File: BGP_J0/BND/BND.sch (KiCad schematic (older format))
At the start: 5 parts, among them J1 Conn_01x13, J2 Conn_01x03, J4 Conn_01x02, J5 Conn_01x03, P7 CONN_01X04

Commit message: Updates
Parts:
- P7: footprint (none) -> Connectors_JST:JST_PH_B4B-PH-K_04x2.00mm_Straight
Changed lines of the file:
@@
 	5450 3950 5200 3950
 $Comp
-L Earth #PWR03
+L Earth #PWR01
 U 1 1 5AE4ECAD
 P 5200 4650
-F 0 "#PWR03" H 5200 4400 50  0001 C CNN
+F 0 "#PWR01" H 5200 4400 50  0001 C CNN
 F 1 "Earth" H 5200 4500 50  0001 C CNN
 F 2 "" H 5200 4650 50  0001 C CNN
@@
 BT_O
 $Comp
-L Earth #PWR04
+L Earth #PWR02
 U 1 1 5AE4F0BF
 P 6600 4250
-F 0 "#PWR04" H 6600 4000 50  0001 C CNN
+F 0 "#PWR02" H 6600 4000 50  0001 C CNN
 F 1 "Earth" H 6600 4100 50  0001 C CNN
 F 2 "" H 6600 4250 50  0001 C CNN
@@
 $EndComp
 $Comp
-L Earth #PWR05
+L Earth #PWR03
 U 1 1 5AE533F6
 P 6050 3450
-F 0 "#PWR05" H 6050 3200 50  0001 C CNN
+F 0 "#PWR03" H 6050 3200 50  0001 C CNN
 F 1 "Earth" H 6050 3300 50  0001 C CNN
 F 2 "" H 6050 3450 50  0001 C CNN
@@
 $EndComp
 $Comp
-L Earth #PWR06
+L Earth #PWR04
 U 1 1 5AE53416
 P 6600 3650
-F 0 "#PWR06" H 6600 3400 50  0001 C CNN
+F 0 "#PWR04" H 6600 3400 50  0001 C CNN
 F 1 "Earth" H 6600 3500 50  0001 C CNN
 F 2 "" H 6600 3650 50  0001 C CNN
@@
 F 0 "P7" H 6400 4350 50  0000 C CNN
 F 1 "CONN_01X04" H 6400 3850 50  0000 C CNN
-F 2 "" H 6400 4100 50  0000 C CNN
+F 2 "Connectors_JST:JST_PH_B4B-PH-K_04x2.00mm_Straight" H 6400 4100 50  0001 C CNN
 F 3 "" H 6400 4100 50  0000 C CNN
 	1    6400 4100

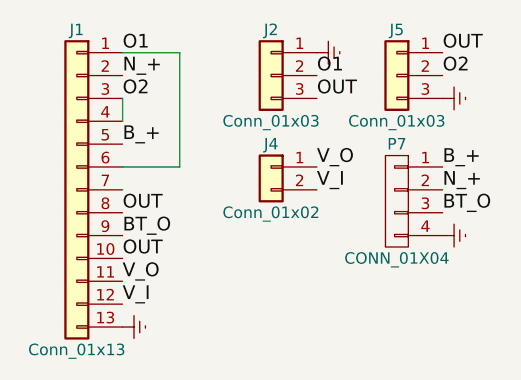
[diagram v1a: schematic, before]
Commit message: Ready to go
Reverted J0_BND  to include P/U inputs
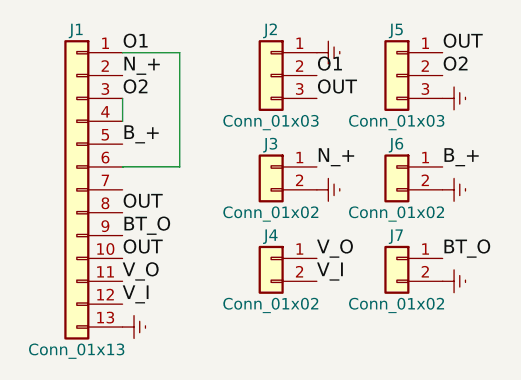
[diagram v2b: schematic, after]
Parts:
- removed P7: CONN_01X04, Connectors_JST:JST_PH_B4B-PH-K_04x2.00mm_Straight, symbol CONN_01X04
- added J3, J6: Conn_01x02, LIBS:TerminalBlock_Phoenix_MPT-2.54mm_2pol, symbol Conn_01x02
- added J7: Conn_01x02, Connectors_JST:JST_PH_B2B-PH-K_02x2.00mm_Straight, symbol Conn_01x02
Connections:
- net BT_O: now also J7.1 (Pin_1)
- net B_+: now also J6.1 (Pin_1)
- net Earth: now also J3.2 (Pin_2), J6.2 (Pin_2), J7.2 (Pin_2)
- net N_+: now also J3.1 (Pin_1)
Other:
- moved on the sheet: J4
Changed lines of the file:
@@
 LIBS:switches
 LIBS:relays
+LIBS:motors
 LIBS:transistors
 LIBS:conn
@@
 	-1   0    0    -1
 $EndComp
-Text Label 6600 4050 0    60   ~ 0
+$Comp
+L Conn_01x02 J3
+U 1 1 5AE4EB53
+P 5850 3950
+F 0 "J3" H 5850 4050 50  0000 C CNN
+F 1 "Conn_01x02" H 5850 3750 50  0000 C CNN
+F 2 "LIBS:TerminalBlock_Phoenix_MPT-2.54mm_2pol" H 5850 3950 50  0001 C CNN
+F 3 "" H 5850 3950 50  0001 C CNN
+	1    5850 3950
+	-1   0    0    -1
+$EndComp
+$Comp
+L Conn_01x02 J6
+U 1 1 5AE4EB86
+P 6400 3950
+F 0 "J6" H 6400 4050 50  0000 C CNN
+F 1 "Conn_01x02" H 6400 3750 50  0000 C CNN
+F 2 "LIBS:TerminalBlock_Phoenix_MPT-2.54mm_2pol" H 6400 3950 50  0001 C CNN
+F 3 "" H 6400 3950 50  0001 C CNN
+	1    6400 3950
+	-1   0    0    -1
+$EndComp
+Text Label 6050 3950 0    60   ~ 0
 N_+
 Text Label 5200 3550 0    60   ~ 0
 N_+
+$Comp
+L Earth #PWR01
+U 1 1 5AE4EC05
+P 6050 4050
+F 0 "#PWR01" H 6050 3800 50  0001 C CNN
+F 1 "Earth" H 6050 3900 50  0001 C CNN
+F 2 "" H 6050 4050 50  0001 C CNN
+F 3 "" H 6050 4050 50  0001 C CNN
+	1    6050 4050
+	0    -1   1    0
+$EndComp
+$Comp
+L Earth #PWR02
+U 1 1 5AE4EC20
+P 6600 4050
+F 0 "#PWR02" H 6600 3800 50  0001 C CNN
+F 1 "Earth" H 6600 3900 50  0001 C CNN
+F 2 "" H 6600 4050 50  0001 C CNN
+F 3 "" H 6600 4050 50  0001 C CNN
+	1    6600 4050
+	0    -1   1    0
+$EndComp
 Wire Wire Line
 	5200 3650 5200 3750
@@
 	5450 3950 5200 3950
 $Comp
-L Earth #PWR01
+L Earth #PWR03
 U 1 1 5AE4ECAD
 P 5200 4650
-F 0 "#PWR01" H 5200 4400 50  0001 C CNN
+F 0 "#PWR03" H 5200 4400 50  0001 C CNN
 F 1 "Earth" H 5200 4500 50  0001 C CNN
 F 2 "" H 5200 4650 50  0001 C CNN
@@
 L Conn_01x02 J4
 U 1 1 5AE4EEB8
-P 5850 3950
-F 0 "J4" H 5850 4050 50  0000 C CNN
-F 1 "Conn_01x02" H 5850 3750 50  0000 C CNN
-F 2 "Connectors_JST:JST_PH_B2B-PH-K_02x2.00mm_Straight" H 5850 3950 50  0001 C CNN
-F 3 "" H 5850 3950 50  0001 C CNN
-	1    5850 3950
-	-1   0    0    -1
-$EndComp
-Text Label 6050 4050 0    60   ~ 0
+P 5850 4350
+F 0 "J4" H 5850 4450 50  0000 C CNN
+F 1 "Conn_01x02" H 5850 4150 50  0000 C CNN
+F 2 "Connectors_JST:JST_PH_B2B-PH-K_02x2.00mm_Straight" H 5850 4350 50  0001 C CNN
+F 3 "" H 5850 4350 50  0001 C CNN
+	1    5850 4350
+	-1   0    0    -1
+$EndComp
+Text Label 6050 4450 0    60   ~ 0
 V_I
-Text Label 6050 3950 0    60   ~ 0
+Text Label 6050 4350 0    60   ~ 0
 V_O
-Text Label 6600 4150 0    60   ~ 0
+$Comp
+L Conn_01x02 J7
+U 1 1 5AE4F048
+P 6400 4350
+F 0 "J7" H 6400 4450 50  0000 C CNN
+F 1 "Conn_01x02" H 6400 4150 50  0000 C CNN
+F 2 "Connectors_JST:JST_PH_B2B-PH-K_02x2.00mm_Straight" H 6400 4350 50  0001 C CNN
+F 3 "" H 6400 4350 50  0001 C CNN
+	1    6400 4350
+	-1   0    0    -1
+$EndComp
+Text Label 6600 4350 0    60   ~ 0
 BT_O
 $Comp
-L Earth #PWR02
+L Earth #PWR04
 U 1 1 5AE4F0BF
-P 6600 4250
-F 0 "#PWR02" H 6600 4000 50  0001 C CNN
-F 1 "Earth" H 6600 4100 50  0001 C CNN
-F 2 "" H 6600 4250 50  0001 C CNN
-F 3 "" H 6600 4250 50  0001 C CNN
-	1    6600 4250
+P 6600 4450
+F 0 "#PWR04" H 6600 4200 50  0001 C CNN
+F 1 "Earth" H 6600 4300 50  0001 C CNN
+F 2 "" H 6600 4450 50  0001 C CNN
+F 3 "" H 6600 4450 50  0001 C CNN
+	1    6600 4450
 	0    -1   -1   0
 $EndComp
@@
 $EndComp
 $Comp
-L Earth #PWR03
+L Earth #PWR05
 U 1 1 5AE533F6
 P 6050 3450
-F 0 "#PWR03" H 6050 3200 50  0001 C CNN
+F 0 "#PWR05" H 6050 3200 50  0001 C CNN
 F 1 "Earth" H 6050 3300 50  0001 C CNN
 F 2 "" H 6050 3450 50  0001 C CNN
@@
 $EndComp
 $Comp
-L Earth #PWR04
+L Earth #PWR06
 U 1 1 5AE53416
 P 6600 3650
-F 0 "#PWR04" H 6600 3400 50  0001 C CNN
+F 0 "#PWR06" H 6600 3400 50  0001 C CNN
 F 1 "Earth" H 6600 3500 50  0001 C CNN
 F 2 "" H 6600 3650 50  0001 C CNN
@@
 Text Label 6600 3550 0    60   ~ 0
 O2
-$Comp
-L CONN_01X04 P7
-U 1 1 5AE6AC54
-P 6400 4100
-F 0 "P7" H 6400 4350 50  0000 C CNN
-F 1 "CONN_01X04" H 6400 3850 50  0000 C CNN
-F 2 "Connectors_JST:JST_PH_B4B-PH-K_04x2.00mm_Straight" H 6400 4100 50  0001 C CNN
-F 3 "" H 6400 4100 50  0000 C CNN
-	1    6400 4100
-	-1   0    0    -1
-$EndComp
 $EndSCHEMATC

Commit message: Gerbers fixed - ready to go
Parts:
- removed J3, J6: Conn_01x02, LIBS:TerminalBlock_Phoenix_MPT-2.54mm_2pol, symbol Conn_01x02
- removed J7: Conn_01x02, Connectors_JST:JST_PH_B2B-PH-K_02x2.00mm_Straight, symbol Conn_01x02
- added P7: CONN_01X04, symbol CONN_01X04
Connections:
- net BT_O: now also P7.3 (P3)
- net B_+: now also P7.1 (P1)
- net Earth: now also P7.4 (P4)
- net N_+: now also P7.2 (P2)
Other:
- moved on the sheet: J4
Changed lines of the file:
@@
 LIBS:switches
 LIBS:relays
-LIBS:motors
 LIBS:transistors
 LIBS:conn
@@
 	-1   0    0    -1
 $EndComp
-$Comp
-L Conn_01x02 J3
-U 1 1 5AE4EB53
-P 5850 3950
-F 0 "J3" H 5850 4050 50  0000 C CNN
-F 1 "Conn_01x02" H 5850 3750 50  0000 C CNN
-F 2 "LIBS:TerminalBlock_Phoenix_MPT-2.54mm_2pol" H 5850 3950 50  0001 C CNN
-F 3 "" H 5850 3950 50  0001 C CNN
-	1    5850 3950
-	-1   0    0    -1
-$EndComp
-$Comp
-L Conn_01x02 J6
-U 1 1 5AE4EB86
-P 6400 3950
-F 0 "J6" H 6400 4050 50  0000 C CNN
-F 1 "Conn_01x02" H 6400 3750 50  0000 C CNN
-F 2 "LIBS:TerminalBlock_Phoenix_MPT-2.54mm_2pol" H 6400 3950 50  0001 C CNN
-F 3 "" H 6400 3950 50  0001 C CNN
-	1    6400 3950
-	-1   0    0    -1
-$EndComp
-Text Label 6050 3950 0    60   ~ 0
+Text Label 6600 4050 0    60   ~ 0
 N_+
 Text Label 5200 3550 0    60   ~ 0
 N_+
-$Comp
-L Earth #PWR01
-U 1 1 5AE4EC05
-P 6050 4050
-F 0 "#PWR01" H 6050 3800 50  0001 C CNN
-F 1 "Earth" H 6050 3900 50  0001 C CNN
-F 2 "" H 6050 4050 50  0001 C CNN
-F 3 "" H 6050 4050 50  0001 C CNN
-	1    6050 4050
-	0    -1   1    0
-$EndComp
-$Comp
-L Earth #PWR02
-U 1 1 5AE4EC20
-P 6600 4050
-F 0 "#PWR02" H 6600 3800 50  0001 C CNN
-F 1 "Earth" H 6600 3900 50  0001 C CNN
-F 2 "" H 6600 4050 50  0001 C CNN
-F 3 "" H 6600 4050 50  0001 C CNN
-	1    6600 4050
-	0    -1   1    0
-$EndComp
 Wire Wire Line
 	5200 3650 5200 3750
@@
 L Conn_01x02 J4
 U 1 1 5AE4EEB8
-P 5850 4350
-F 0 "J4" H 5850 4450 50  0000 C CNN
-F 1 "Conn_01x02" H 5850 4150 50  0000 C CNN
-F 2 "Connectors_JST:JST_PH_B2B-PH-K_02x2.00mm_Straight" H 5850 4350 50  0001 C CNN
-F 3 "" H 5850 4350 50  0001 C CNN
-	1    5850 4350
+P 5850 3950
+F 0 "J4" H 5850 4050 50  0000 C CNN
+F 1 "Conn_01x02" H 5850 3750 50  0000 C CNN
+F 2 "Connectors_JST:JST_PH_B2B-PH-K_02x2.00mm_Straight" H 5850 3950 50  0001 C CNN
+F 3 "" H 5850 3950 50  0001 C CNN
+	1    5850 3950
 	-1   0    0    -1
 $EndComp
-Text Label 6050 4450 0    60   ~ 0
+Text Label 6050 4050 0    60   ~ 0
 V_I
-Text Label 6050 4350 0    60   ~ 0
+Text Label 6050 3950 0    60   ~ 0
 V_O
-$Comp
-L Conn_01x02 J7
-U 1 1 5AE4F048
-P 6400 4350
-F 0 "J7" H 6400 4450 50  0000 C CNN
-F 1 "Conn_01x02" H 6400 4150 50  0000 C CNN
-F 2 "Connectors_JST:JST_PH_B2B-PH-K_02x2.00mm_Straight" H 6400 4350 50  0001 C CNN
-F 3 "" H 6400 4350 50  0001 C CNN
-	1    6400 4350
-	-1   0    0    -1
-$EndComp
-Text Label 6600 4350 0    60   ~ 0
+Text Label 6600 4150 0    60   ~ 0
 BT_O
 $Comp
 L Earth #PWR04
 U 1 1 5AE4F0BF
-P 6600 4450
-F 0 "#PWR04" H 6600 4200 50  0001 C CNN
-F 1 "Earth" H 6600 4300 50  0001 C CNN
-F 2 "" H 6600 4450 50  0001 C CNN
-F 3 "" H 6600 4450 50  0001 C CNN
-	1    6600 4450
+P 6600 4250
+F 0 "#PWR04" H 6600 4000 50  0001 C CNN
+F 1 "Earth" H 6600 4100 50  0001 C CNN
+F 2 "" H 6600 4250 50  0001 C CNN
+F 3 "" H 6600 4250 50  0001 C CNN
+	1    6600 4250
 	0    -1   -1   0
 $EndComp
@@
 Text Label 6600 3550 0    60   ~ 0
 O2
+$Comp
+L CONN_01X04 P7
+U 1 1 5AE6AC54
+P 6400 4100
+F 0 "P7" H 6400 4350 50  0000 C CNN
+F 1 "CONN_01X04" H 6400 3850 50  0000 C CNN
+F 2 "" H 6400 4100 50  0000 C CNN
+F 3 "" H 6400 4100 50  0000 C CNN
+	1    6400 4100
+	-1   0    0    -1
+$EndComp
 $EndSCHEMATC
